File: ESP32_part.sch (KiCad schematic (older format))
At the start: 43 parts, among them Q18 UMH3N, Q19 2N5551S, SW2 SW_RST, SW3 SW_FLASH, U10 AT24CS64-XHM, U11 FM24C64B, U8 CH340C, U9 ESP-12F

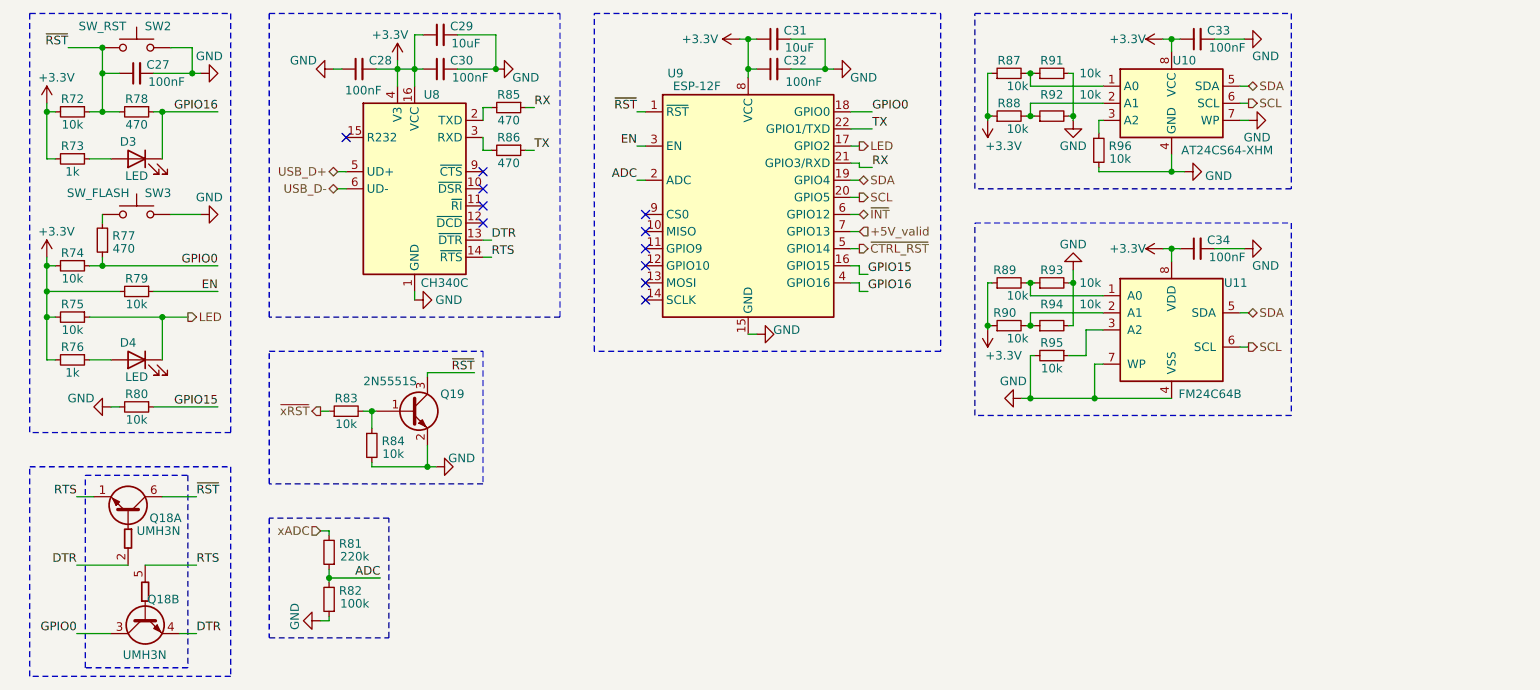
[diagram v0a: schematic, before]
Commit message: Завершена трассировка печатной платы. Исправлены ошибки в схема.
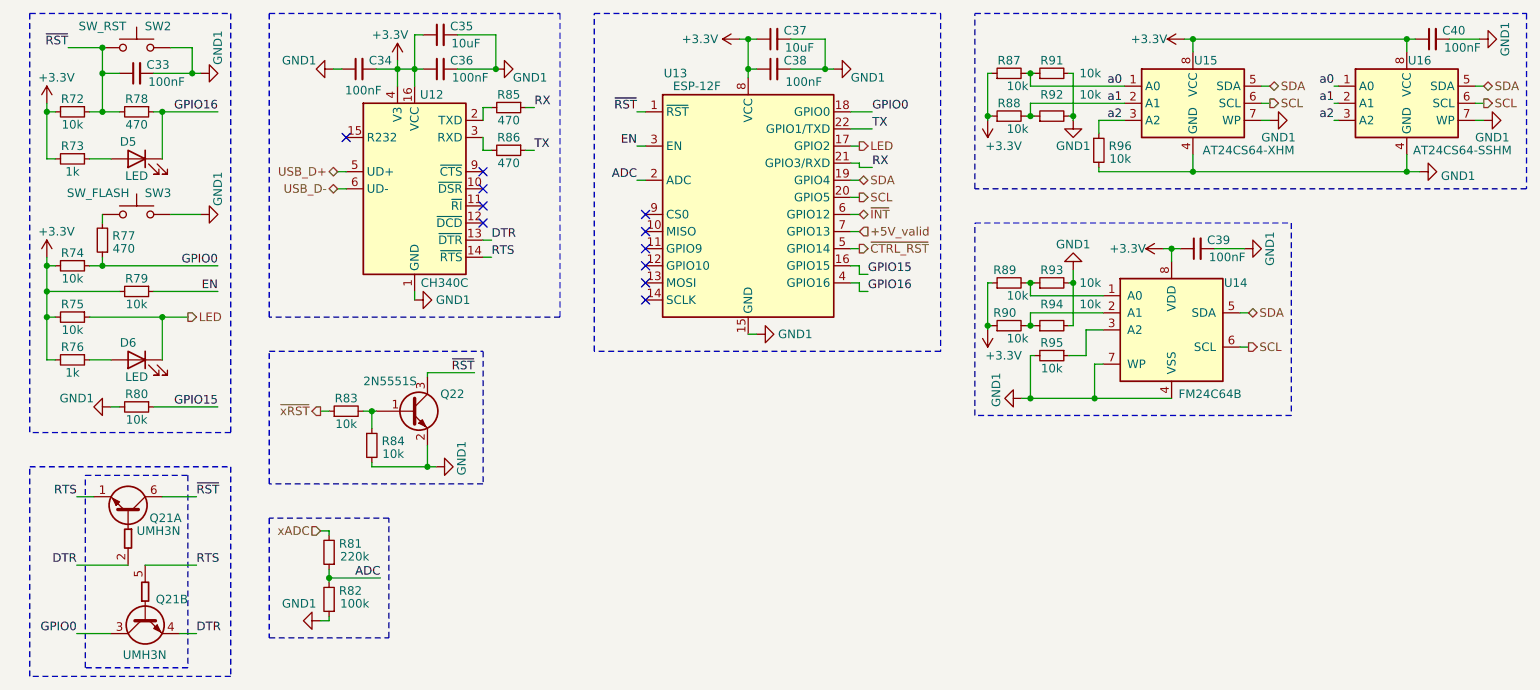
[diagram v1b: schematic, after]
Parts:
- added U16: AT24CS64-SSHM, Package_SO:SOIC-8_3.9x4.9mm_P1.27mm, symbol Memory_EEPROM:AT24CS64-SSHM
- D5: renamed from D3; footprint LED_THT:LED_D1.8mm_W1.8mm_H2.4mm_Horizontal_O1.27mm_Z1.6mm -> LED_SMD:LED_0603_1608Metric
- D6: renamed from D4; footprint LED_THT:LED_D1.8mm_W1.8mm_H2.4mm_Horizontal_O1.27mm_Z1.6mm -> LED_SMD:LED_0603_1608Metric
- renumbered C27 to C33, C28 to C34, C29 to C35, C30 to C36, C31 to C37, C32 to C38, C34 to C39, C33 to C40, Q18 to Q21, Q19 to Q22, U8 to U12, U9 to U13, U11 to U14, U10 to U15
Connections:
- net +3V3: now also U16.8 (VCC)
- net SCL: now also U16.6 (SCL)
- net SDA: now also U16.5 (SDA)
- net a0: now reaches R87.2, R91.1, U15.1 (A0)
- net a0: now also U16.1 (A0)
- net a1: now reaches R88.2, R92.1, U15.2 (A1)
- net a1: now also U16.2 (A1)
- net a2: now reaches R96.1, U15.3 (A2)
- net a2: now also U16.3 (A2)
- net GND renamed GND1
- net GND1: now also U16.4 (GND), U16.7 (WP)
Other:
- moved on the sheet: C40, U15
